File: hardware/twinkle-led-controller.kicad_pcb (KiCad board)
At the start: 4 copper layers, 75 x 61.5 mm, 65 parts, among them J1 USB_B_Micro, J10 Screw_Terminal_01x02, J11 Screw_Terminal_01x02, J12 Screw_Terminal_01x02, J2 Conn_01x05, J3 Screw_Terminal_01x02, J4 Screw_Terminal_01x02, J5 Screw_Terminal_01x02, J6 Screw_Terminal_01x02, J7 Screw_Terminal_01x02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

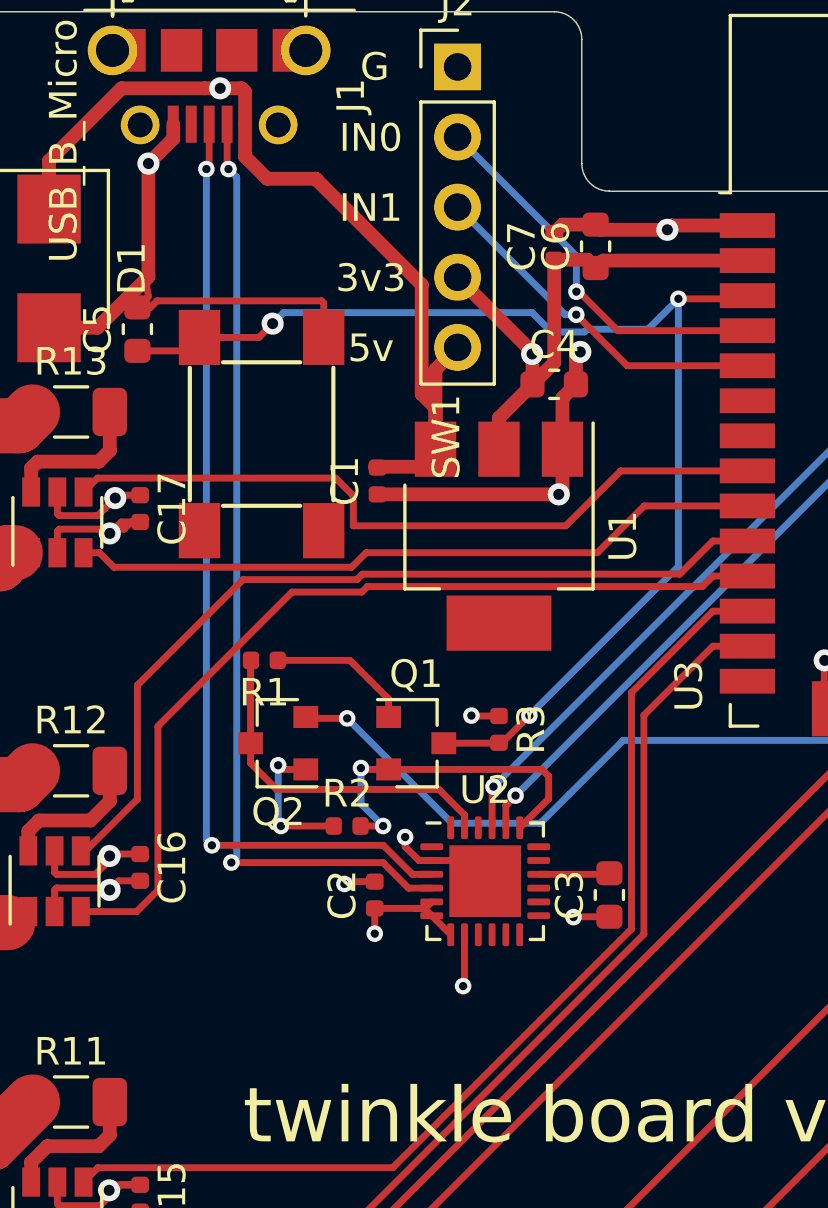
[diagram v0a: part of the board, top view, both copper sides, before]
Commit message: Fix v1.0 layout and generate gerbers/placement files
- Update to CP2102, since JLCPCB doesn't have CP2104
- Fix current-limiting resistors to 10 ohm
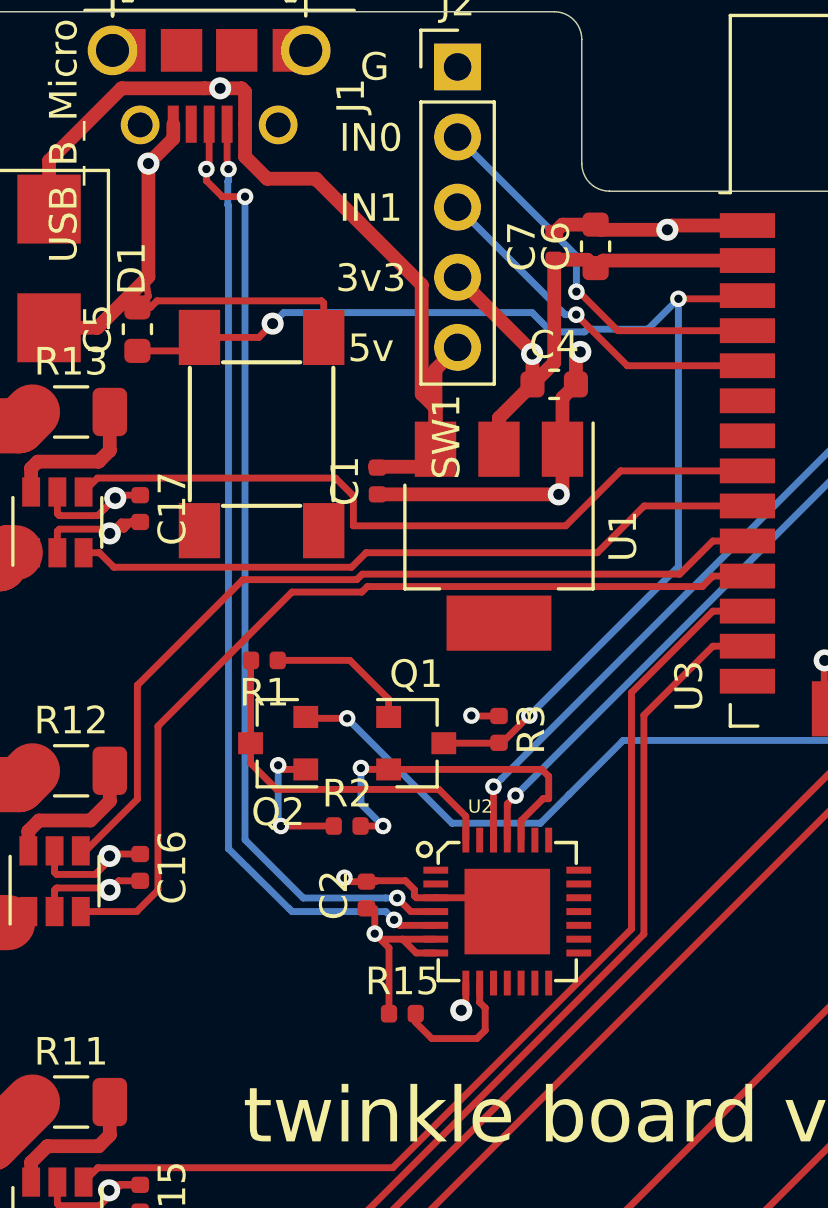
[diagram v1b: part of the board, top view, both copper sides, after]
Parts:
- removed C3: 4.7uF, Capacitor_SMD:C_0603_1608Metric
- added R15: 10k, Resistor_SMD:R_0402_1005Metric, F.Cu at (201.0, 88.3)
- R10, R11, R12, R13, R4, R5, R6, R7, R8, R9: value 180 -> 10
- U2: value CP2104 -> INTERFACE-CP2102-GMR(QFN28); footprint Package_DFN_QFN:QFN-24-1EP_4x4mm_P0.5mm_EP2.6x2.6mm -> snapeda:QFN28G_0.5-5X5MM
- moved U2 1.36 mm to (204.8, 84.6)
- moved C2 0.30 mm to (199.7, 84.0)
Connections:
- U2 pad 16: Net-(C3-Pad2) -> (no net)
- U2 pad 19: /USB_RTS -> (no net)
- U2 pad 2: GND -> (no net)
- U2 pad 20: /USB_RX -> (no net)
- U2 pad 21: /USB_TX -> (no net)
- U2 pad 23: /USB_DTR -> (no net)
- U2 pad 24: (no net) -> /USB_RTS
- U2 pad 25: GND -> /USB_RX
- U2 pad 3: /USB_D+ -> GND
- U2 pad 4: /USB_D- -> /USB_D+
- U2 pad 5: +3V3 -> /USB_D-
- U2 pad 9: (no net) -> Net-(R15-Pad2)
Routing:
- net Net-(R15-Pad2): track 0.00 -> 4.99 mm
- net +3V3: track 25.6 -> 28.7 mm
- net Net-(C3-Pad2): track 2.58 -> 0.00 mm
- net +5V: track 78.0 -> 77.2 mm
- net /USB_RTS: track 12.5 -> 13.0 mm
- net /USB_D+: track 34.6 -> 35.0 mm, vias 2 -> 3
- net GND: track 96.3 -> 96.7 mm, vias 22 -> 20

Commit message: Hardware revision 1.1:
- Fix pins to not use flash pins
- Fix screw terminal footprint (holes were too small)
- Add screw terminal for power
- Add out for multi-unit synchronization
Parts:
- removed C17: 0.1uF, Capacitor_SMD:C_0402_1005Metric
- removed R13: 10, Resistor_SMD:R_1206_3216Metric
- removed U13: HT7K1201, Package_TO_SOT_SMD:SOT-23-6
- moved J12 1.50 mm to (182.0, 65.5)
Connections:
- net /AUX0 renamed /AUX_IN
- D2 pad 2: /LED_BUILTIN -> /AUX_OUT
- J12 pad 1: Net-(J12-Pad1) -> +5V
- J12 pad 2: Net-(J12-Pad2) -> GND
- J2 pad 3: /AUX1 -> /AUX_OUT
- U3 pad 10: /LED8_A -> /LED7_A
- U3 pad 11: /LED8_B -> /LED7_B
- U3 pad 12: /LED7_A -> /LED6_A
- U3 pad 13: /LED7_B -> /LED6_B
- U3 pad 14: (no net) -> /AUX_OUT
- U3 pad 16: /LED6_A -> /LED5_A
- U3 pad 17: /LED6_B -> (no net)
- U3 pad 18: /LED5_A -> (no net)
- U3 pad 19: /LED_BUILTIN -> (no net)
- U3 pad 20: /LED5_B -> (no net)
- U3 pad 21: /LED4_A -> (no net)
- U3 pad 22: /LED4_B -> (no net)
- U3 pad 23: (no net) -> /LED5_B
- U3 pad 24: (no net) -> /LED4_A
- U3 pad 26: /LED3_A -> /LED4_B
- U3 pad 27: /LED3_B -> /LED3_A
- U3 pad 28: /LED2_A -> /LED3_B
- U3 pad 29: (no net) -> /LED2_A
- U3 pad 5: /AUX1 -> (no net)
- U3 pad 8: /LED9_A -> /LED8_A
- U3 pad 9: /LED9_B -> /LED8_B
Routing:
- net /AUX_OUT: track 0.00 -> 46.0 mm, vias 0 -> 3
- net /LED9_A: track 26.4 -> 0.00 mm
- net /LED9_B: track 25.2 -> 0.00 mm
- net /AUX1: track 12.9 -> 0.00 mm, vias 1 -> 0
- net /LED_BUILTIN: track 6.51 -> 0.00 mm
- net Net-(J12-Pad1): track 5.81 -> 0.00 mm
- net Net-(R13-Pad2): track 5.38 -> 0.00 mm
- net Net-(J12-Pad2): track 5.20 -> 0.00 mm
- net /LED4_B: track 24.1 -> 28.8 mm
- net +5V: track 77.2 -> 81.9 mm, vias 12 -> 11
- net GND: track 96.7 -> 101.1 mm, vias 20 -> 19
- net /LED8_B: track 32.7 -> 36.4 mm
- net /LED5_B: track 29.4 -> 32.7 mm
- net /LED7_B: track 37.7 -> 40.9 mm
- net /LED6_A: track 33.7 -> 36.4 mm
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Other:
- board text added: "5V"
- board text added: "IN"
- board text added: "OUT"
- board text added: "twinkle board v1.1"
- board text removed: "9"
- board text removed: "IN0"
- board text removed: "IN1"
- board text removed: "twinkle board v1.0"
